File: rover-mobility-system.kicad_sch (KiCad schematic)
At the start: 0 parts

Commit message: update: file move
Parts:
- added J1: CH1_PH_6Pin, S6B-PH-SM4TB__SN_:S6B-PH-SM4-TB_LF__SN__3, symbol S6B-PH-SM4-TB_LF__SN_:S6B-PH-SM4-TB
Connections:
- new net +3.3V: J1.2
- new net CH1_OUT1: J1.1
- new net CH1_OUT2: J1.6
- new net CH1_Phase_A: J1.3
- new net CH1_Phase_B: J1.4
- new net GND: J1.5
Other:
- note added: "Encoder GND"
- note added: "Encoder VCC"
- note added: "Motor +"
- note added: "Motor -"
- note added: "Phase A"
- note added: "Phase B"

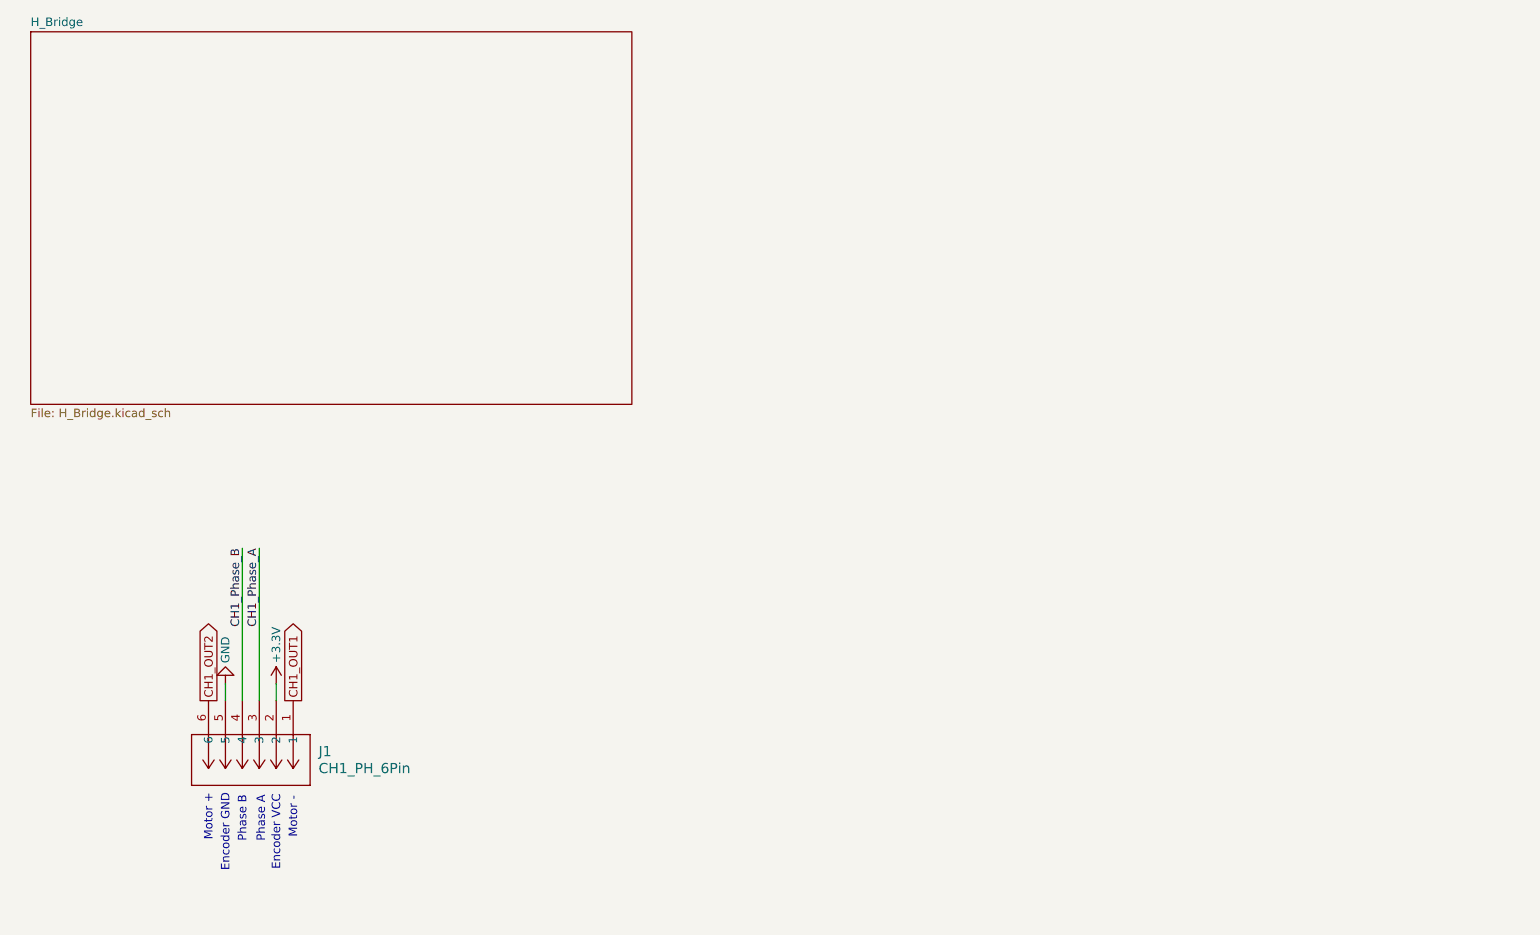
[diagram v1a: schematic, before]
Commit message: add w5500 schematic
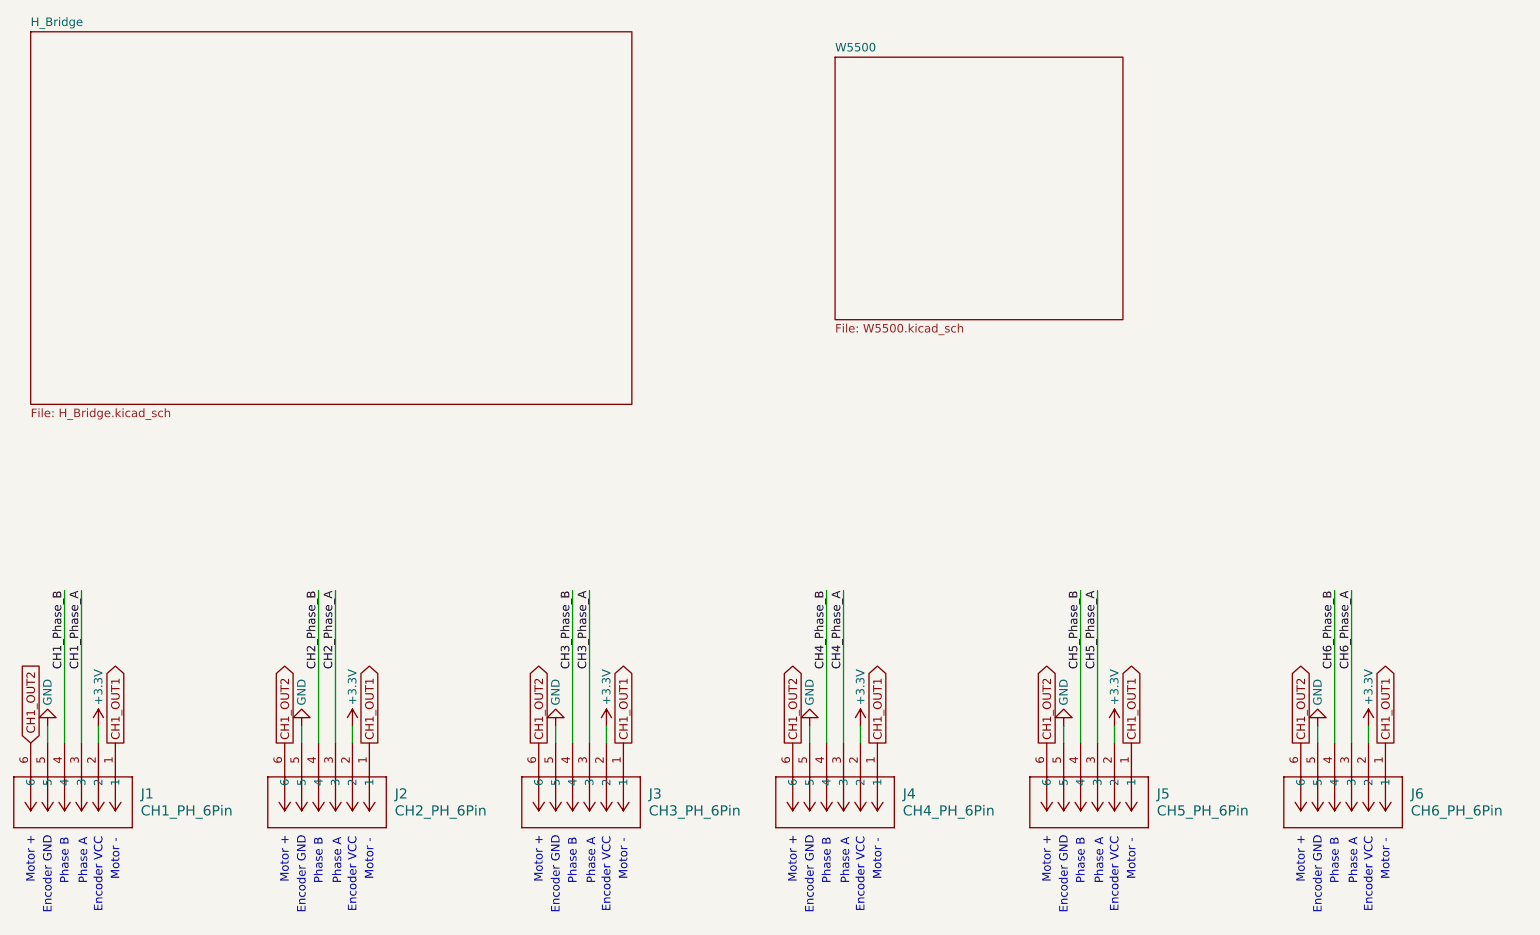
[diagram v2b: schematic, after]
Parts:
- added J2: CH2_PH_6Pin, S6B-PH-SM4TB__SN_:S6B-PH-SM4-TB_LF__SN__3, symbol S6B-PH-SM4-TB_LF__SN_:S6B-PH-SM4-TB
- added J3: CH3_PH_6Pin, S6B-PH-SM4TB__SN_:S6B-PH-SM4-TB_LF__SN__3, symbol S6B-PH-SM4-TB_LF__SN_:S6B-PH-SM4-TB
- added J4: CH4_PH_6Pin, S6B-PH-SM4TB__SN_:S6B-PH-SM4-TB_LF__SN__3, symbol S6B-PH-SM4-TB_LF__SN_:S6B-PH-SM4-TB
- added J5: CH5_PH_6Pin, S6B-PH-SM4TB__SN_:S6B-PH-SM4-TB_LF__SN__3, symbol S6B-PH-SM4-TB_LF__SN_:S6B-PH-SM4-TB
- added J6: CH6_PH_6Pin, S6B-PH-SM4TB__SN_:S6B-PH-SM4-TB_LF__SN__3, symbol S6B-PH-SM4-TB_LF__SN_:S6B-PH-SM4-TB
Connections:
- net +3.3V: now also J2.2, J3.2, J4.2, J5.2, J6.2
- net CH1_OUT1: now also J2.1, J3.1, J4.1, J5.1, J6.1
- net CH1_OUT2: now also J2.6, J3.6, J4.6, J5.6, J6.6
- net GND: now also J2.5, J3.5, J4.5, J5.5, J6.5
- new net CH2_Phase_A: J2.3
- new net CH2_Phase_B: J2.4
- new net CH3_Phase_A: J3.3
- new net CH3_Phase_B: J3.4
- new net CH4_Phase_A: J4.3
- new net CH4_Phase_B: J4.4
- new net CH5_Phase_A: J5.3
- new net CH5_Phase_B: J5.4
- new net CH6_Phase_A: J6.3
- new net CH6_Phase_B: J6.4
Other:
- added sheet W5500 (W5500.kicad_sch)
- moved on the sheet: J1
